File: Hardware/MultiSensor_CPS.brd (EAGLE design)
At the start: 100 x 80 mm, 38 parts, among them U1 TCA9548APWR

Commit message: prelim routing
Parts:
- moved SJ1 31.1 mm to (10.0, 3.84), turned to 90 degrees
- moved SJ2 27.9 mm to (12.3, 3.84), turned to 90 degrees
- moved SJ3 24.5 mm to (14.8, 3.94), turned to 90 degrees
- moved SJ5 24.1 mm to (10.8, 18.1), turned to 90 degrees
- moved JP1 21.3 mm to (11.8, 25.9)
- moved SJ4 20.8 mm to (13.1, 18.1), turned to 90 degrees
- moved R16 20.5 mm to (19.7, 18.9)
- moved R14 20.4 mm to (19.8, 13.8)
- moved R17 20.4 mm to (8.18, 21.4)
- moved R3 20.3 mm to (4.52, 14.0)
- moved R7 20.1 mm to (4.32, 4.41)
- moved R10 19.9 mm to (19.8, 4.41)
- moved R20 19.4 mm to (14.7, 7.48), turned to 270 degrees
- moved R19 19.3 mm to (12.4, 7.48), turned to 270 degrees
- moved B1 18.8 mm to (4.42, 14.6)
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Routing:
- net VCC: track 0.00 -> 192.7 mm, vias 0 -> 4
- net SDA: track 0.00 -> 22.7 mm, vias 0 -> 1
- net SCL: track 0.00 -> 22.6 mm
- net SD6: track 0.00 -> 21.4 mm, vias 0 -> 2
- net SC0: track 0.00 -> 19.5 mm, vias 0 -> 2
- net A0: track 0.00 -> 18.8 mm, vias 0 -> 1
- net SC6: track 0.00 -> 17.6 mm, vias 0 -> 1
- net SC4: track 0.00 -> 17.0 mm, vias 0 -> 2
- net A1: track 0.00 -> 14.0 mm, vias 0 -> 1
- net SC7: track 0.00 -> 13.6 mm, vias 0 -> 2
- net SD0: track 0.00 -> 13.1 mm, vias 0 -> 1
- net SD4: track 0.00 -> 12.1 mm, vias 0 -> 2
- net A2: track 0.00 -> 12.1 mm, vias 0 -> 1
- net SD7: track 0.00 -> 11.8 mm, vias 0 -> 1
- net SC2: track 0.00 -> 10.3 mm, vias 0 -> 2
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- added copper zone on layer 1, net GND
- added copper zone on layer 16, net GND
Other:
- board size 100 x 80 mm -> 25 x 29 mm

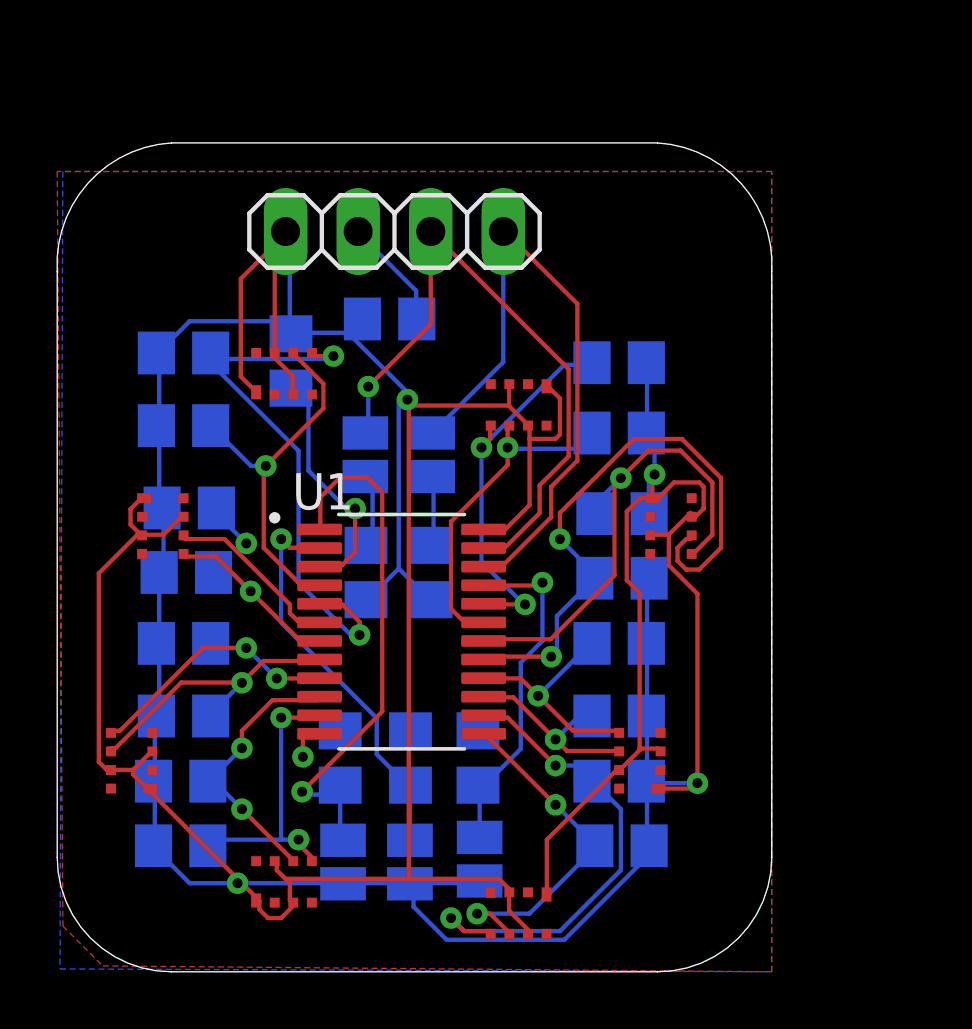
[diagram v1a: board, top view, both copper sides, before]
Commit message: added bypass caps, routing undone
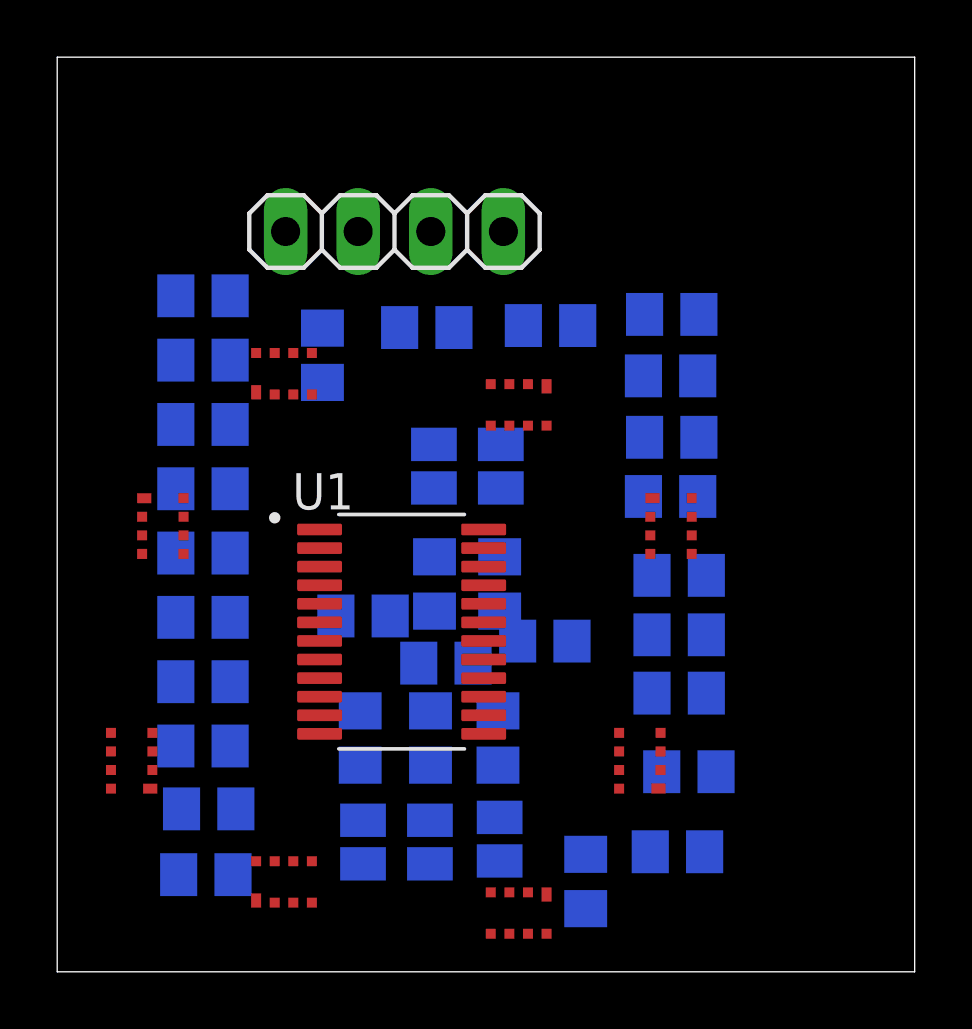
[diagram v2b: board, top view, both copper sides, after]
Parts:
- added C2, C3, C4, C5, C6, C7, C8, C9: 0.1uF, rcl:C0805
- moved R7 11.3 mm to (13.6, 10.8), turned to 180 degrees
- moved R8 8.61 mm to (10.7, 12.4)
- moved R9 5.55 mm to (17.1, 11.6)
- moved R15 2.73 mm to (17.3, 22.6)
- moved R16 2.69 mm to (21.5, 20.9)
- moved R21 2.43 mm to (15.5, 13.6)
- moved SJ4 2.43 mm to (15.5, 17.7)
- moved SJ5 2.43 mm to (13.2, 17.7)
- moved R22 2.43 mm to (13.2, 13.6)
- moved R2 2.31 mm to (5.10, 16.9)
- moved R12 2.25 mm to (21.8, 9.75)
- moved R11 2.12 mm to (21.8, 11.8)
- moved R1 2.11 mm to (5.10, 23.6)
- moved R14 2.00 mm to (21.8, 13.9)
- moved R13 1.80 mm to (21.5, 16.6)
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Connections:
- net GND: now also C2.2, C3.2, C4.2, C5.2, C6.2, C7.2, C8.2, C9.2
- net VCC: now also C2.1, C3.1, C4.1, C5.1, C6.1, C7.1, C8.1, C9.1
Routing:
- net VCC: track 192.7 -> 0.00 mm, vias 4 -> 0
- net SDA: track 22.7 -> 0.00 mm, vias 1 -> 0
- net SCL: track 22.6 -> 0.00 mm
- net SD6: track 21.4 -> 0.00 mm, vias 2 -> 0
- net SC0: track 19.5 -> 0.00 mm, vias 2 -> 0
- net A0: track 18.8 -> 0.00 mm, vias 1 -> 0
- net SC6: track 17.6 -> 0.00 mm, vias 1 -> 0
- net SC4: track 17.0 -> 0.00 mm, vias 2 -> 0
- net A1: track 14.0 -> 0.00 mm, vias 1 -> 0
- net SC7: track 13.6 -> 0.00 mm, vias 2 -> 0
- net SD0: track 13.1 -> 0.00 mm, vias 1 -> 0
- net SD4: track 12.1 -> 0.00 mm, vias 2 -> 0
- net A2: track 12.1 -> 0.00 mm, vias 1 -> 0
- net SD7: track 11.8 -> 0.00 mm, vias 1 -> 0
- net SC2: track 10.3 -> 0.00 mm, vias 2 -> 0
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- removed copper zone on layer 1, net GND
- removed copper zone on layer 16, net GND
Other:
- board size 25 x 29 mm -> 30 x 32 mm
